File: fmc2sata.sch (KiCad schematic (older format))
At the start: 61 parts, among them J1 ASP-134488-01, J2 1-2199230-6, J3 te-770829-1, Q1 BSS138APW, Q2 BSS138APW, Q3 DMG2305UX-13, Q4 BSS138APW, U1 TPS565208, U2 TPS565208, Y1 AX3DAF1-150.0000

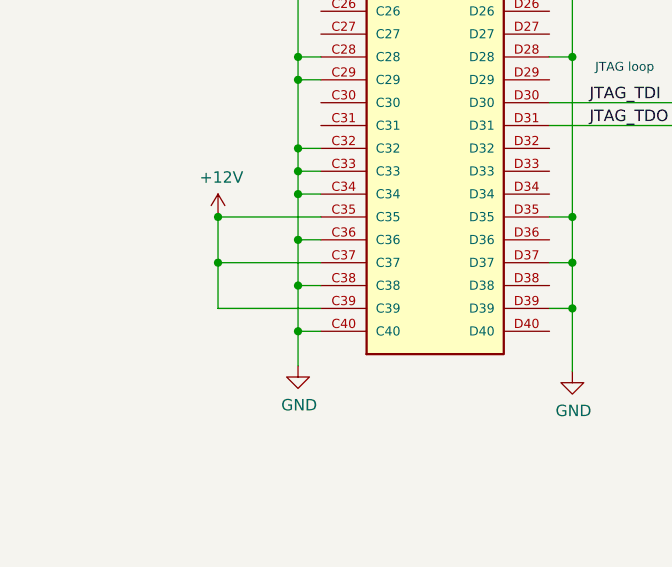
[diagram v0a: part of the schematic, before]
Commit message: Remove C39 connection
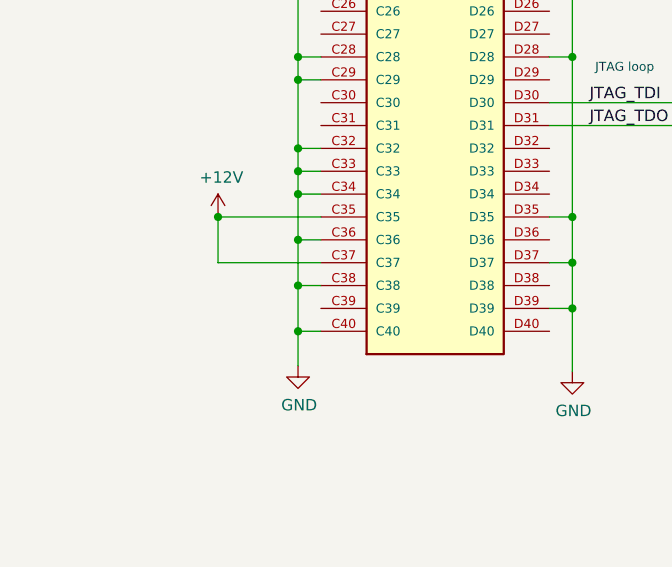
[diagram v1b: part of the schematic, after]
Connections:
- net +12V: no longer J1.C39
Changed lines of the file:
@@
 	1450 6400 1450 6200
 Connection ~ 1450 6200
-Wire Wire Line
-	1900 6600 1450 6600
-Wire Wire Line
-	1450 6600 1450 6400
-Connection ~ 1450 6400
 $Comp
 L fmc2sata:TPS565208 U1

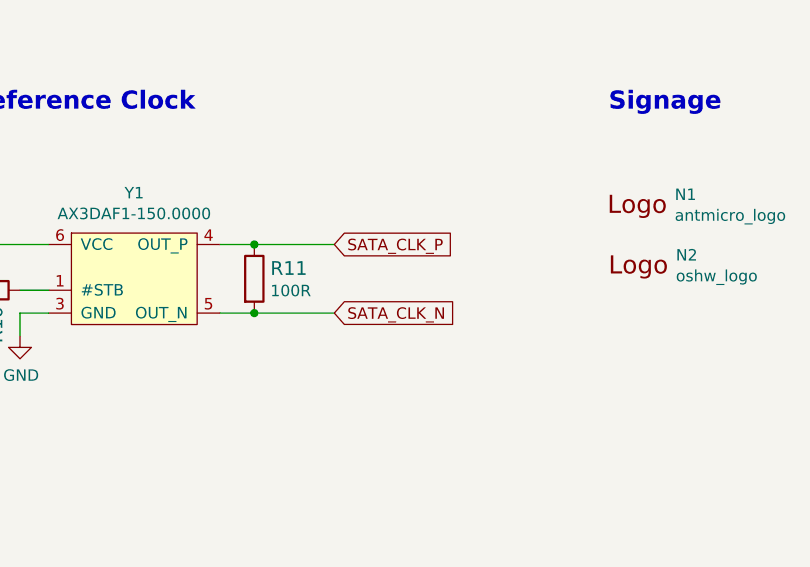
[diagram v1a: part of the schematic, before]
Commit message: Add capacitive coupling to Y1
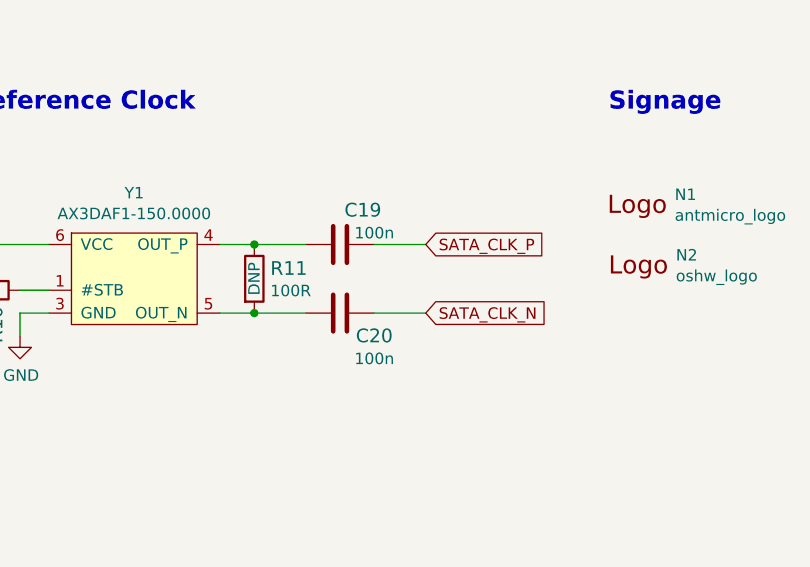
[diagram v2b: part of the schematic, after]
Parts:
- added C19, C20: C_100n_0402, antmicro-footprints:0402-cap, symbol antmicroCapacitors0402:C_100n_0402
- R11: DNP (none) -> DNP
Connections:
- net SATA_CLK_N: now also C20.1; no longer R11.2, Y1.5 (OUT_N)
- net SATA_CLK_P: now also C19.1; no longer R11.1, Y1.4 (OUT_P)
- new net: C19.2, R11.1, Y1.4 (OUT_P)
- new net: C20.2, R11.2, Y1.5 (OUT_N)
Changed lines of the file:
@@
 F 5 "CR0402-FX-1000GLF" H 11850 9825 60  0001 L CNN "MPN"
 F 6 "100R" V 11703 9595 50  0000 L CNN "Val"
+F 7 "DNP" H 11650 9525 50  0000 C CNN "DNP"
 	1    11650 9525
 	0    1    1    0
@@
 Connection ~ 11650 9375
 Wire Wire Line
-	11650 9375 12000 9375
+	11650 9375 11875 9375
 Wire Wire Line
 	11500 9675 11650 9675
 Connection ~ 11650 9675
 Wire Wire Line
-	11650 9675 12000 9675
-Text GLabel 12000 9375 2    50   Input ~ 0
+	11650 9675 11875 9675
+Text GLabel 12400 9375 2    50   Input ~ 0
 SATA_CLK_P
-Text GLabel 12000 9675 2    50   Input ~ 0
+Text GLabel 12400 9675 2    50   Input ~ 0
 SATA_CLK_N
 Text GLabel 11150 4450 2    50   Input ~ 0
@@
 Wire Wire Line
 	7150 7500 7150 7575
+$Comp
+L antmicroCapacitors0402:C_100n_0402 C19
+U 1 1 60245592
+P 12025 9375
+F 0 "C19" V 11875 9475 60  0000 C CNN
+F 1 "C_100n_0402" H 12025 9225 60  0001 C CNN
+F 2 "antmicro-footprints:0402-cap" H 12225 9575 60  0001 L CNN
+F 3 "" H 12025 9375 50  0001 C CNN
+F 4 "Walsin" H 12225 9775 60  0001 L CNN "Manufacturer"
+F 5 "0402X104K6R3CT" H 12225 9675 60  0001 L CNN "MPN"
+F 6 "100n" V 11975 9525 50  0000 C CNN "Val"
+	1    12025 9375
+	0    1    1    0
+$EndComp
+$Comp
+L antmicroCapacitors0402:C_100n_0402 C20
+U 1 1 6024667A
+P 12025 9675
+F 0 "C20" V 12125 9825 60  0000 C CNN
+F 1 "C_100n_0402" H 12025 9525 60  0001 C CNN
+F 2 "antmicro-footprints:0402-cap" H 12225 9875 60  0001 L CNN
+F 3 "" H 12025 9675 50  0001 C CNN
+F 4 "Walsin" H 12225 10075 60  0001 L CNN "Manufacturer"
+F 5 "0402X104K6R3CT" H 12225 9975 60  0001 L CNN "MPN"
+F 6 "100n" V 12225 9825 50  0000 C CNN "Val"
+	1    12025 9675
+	0    1    1    0
+$EndComp
+Wire Wire Line
+	12175 9375 12400 9375
+Wire Wire Line
+	12175 9675 12400 9675
 $EndSCHEMATC

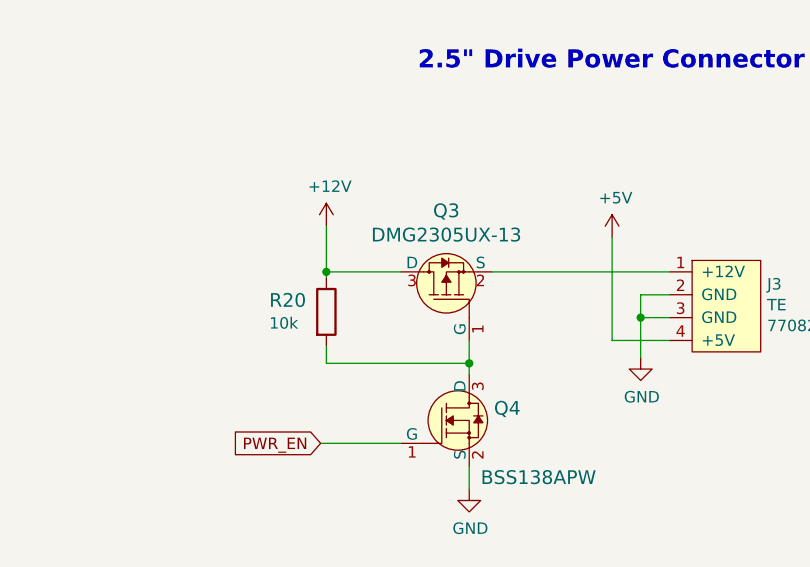
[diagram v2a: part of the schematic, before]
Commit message: Add testpads for power supply - DRC clean
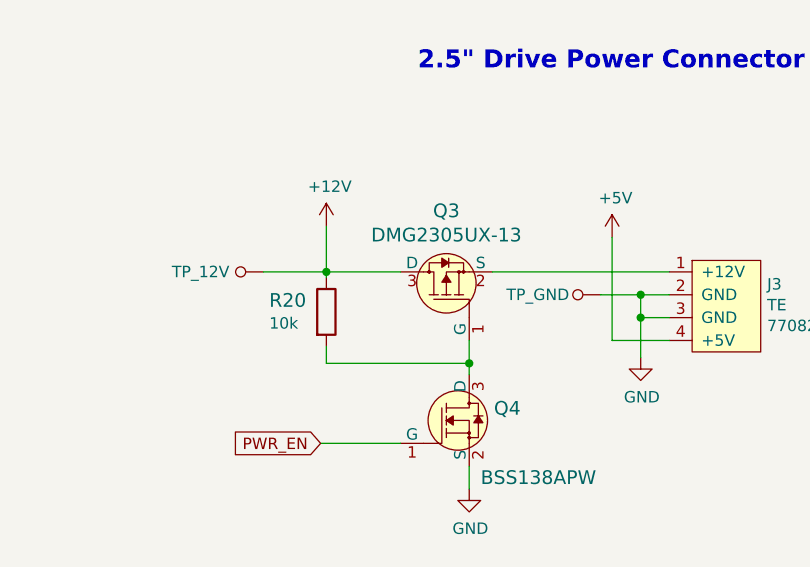
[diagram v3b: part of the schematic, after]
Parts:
- added TP_12V, TP_GND: TP_SMD1MM, antmicro-footprints:Testpoint_smd_1mm, symbol antmicroTestPoints:TP_SMD1MM
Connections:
- net +12V: now also TP_12V.1
- net GND: now also TP_GND.1
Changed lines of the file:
@@
 Wire Wire Line
 	12175 9675 12400 9675
+$Comp
+L antmicroTestPoints:TP_SMD1MM TP_12V
+U 1 1 6032B1A6
+P 12925 3300
+F 0 "TP_12V" V 12925 3125 50  0000 C CNN
+F 1 "TP_SMD1MM" H 12925 3200 50  0001 C CNN
+F 2 "antmicro-footprints:Testpoint_smd_1mm" H 13125 3500 60  0001 L CNN
+F 3 "" H 13125 3600 60  0001 L CNN
+	1    12925 3300
+	0    1    1    0
+$EndComp
+$Comp
+L antmicroTestPoints:TP_SMD1MM TP_GND
+U 1 1 6032C761
+P 14400 3400
+F 0 "TP_GND" V 14400 3225 50  0000 C CNN
+F 1 "TP_SMD1MM" H 14400 3300 50  0001 C CNN
+F 2 "antmicro-footprints:Testpoint_smd_1mm" H 14600 3600 60  0001 L CNN
+F 3 "" H 14600 3700 60  0001 L CNN
+	1    14400 3400
+	0    1    1    0
+$EndComp
+Wire Wire Line
+	14500 3400 14675 3400
+Connection ~ 14675 3400
+Wire Wire Line
+	13025 3300 13300 3300
 $EndSCHEMATC

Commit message: Minor fixes in sch
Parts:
- renumbered TP_12V to TP_12V1, TP_GND to TP_GND1
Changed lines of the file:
@@
 	12175 9675 12400 9675
 $Comp
-L antmicroTestPoints:TP_SMD1MM TP_12V
+L antmicroTestPoints:TP_SMD1MM TP_12V1
 U 1 1 6032B1A6
 P 12925 3300
-F 0 "TP_12V" V 12925 3125 50  0000 C CNN
+F 0 "TP_12V1" V 12925 3125 50  0000 C CNN
 F 1 "TP_SMD1MM" H 12925 3200 50  0001 C CNN
 F 2 "antmicro-footprints:Testpoint_smd_1mm" H 13125 3500 60  0001 L CNN
@@
 $EndComp
 $Comp
-L antmicroTestPoints:TP_SMD1MM TP_GND
+L antmicroTestPoints:TP_SMD1MM TP_GND1
 U 1 1 6032C761
 P 14400 3400
-F 0 "TP_GND" V 14400 3225 50  0000 C CNN
+F 0 "TP_GND1" V 14400 3225 50  0000 C CNN
 F 1 "TP_SMD1MM" H 14400 3300 50  0001 C CNN
 F 2 "antmicro-footprints:Testpoint_smd_1mm" H 14600 3600 60  0001 L CNN
